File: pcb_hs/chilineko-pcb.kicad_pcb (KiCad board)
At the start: 2 copper layers, 303.8 x 94.2 mm, 178 parts, among them J1 JST SH 4-pin, J2 AVR-ISP-6, J3 DATA Breakout, J4 VBUS Breakout, SW1 Reset, U1 SRV05-4, U2 ATmega32U4-AU, Y1 16MHz

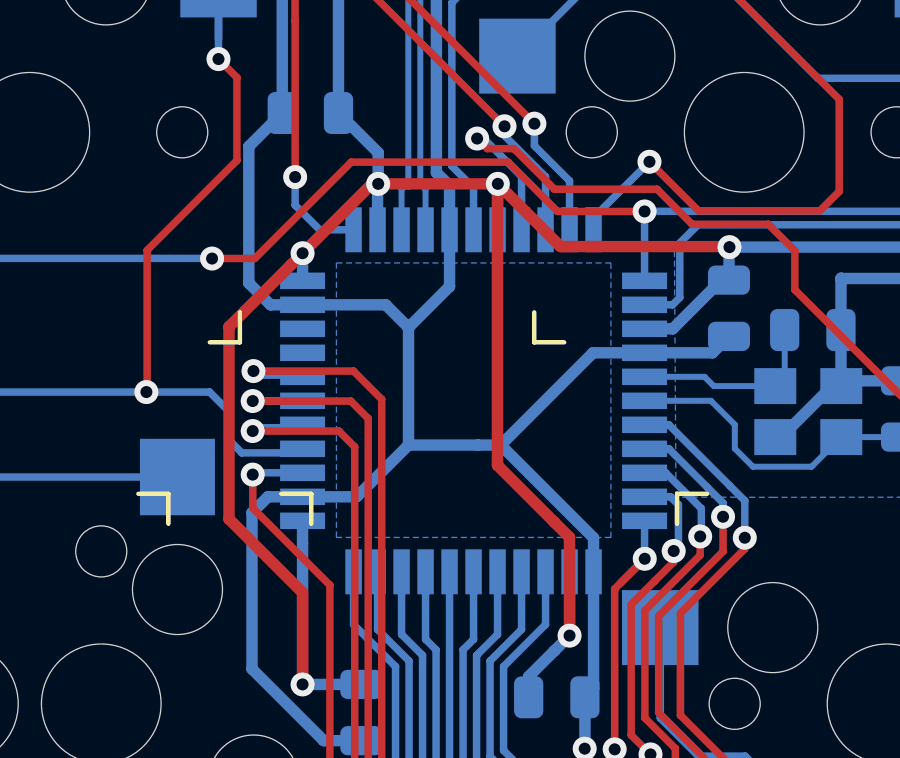
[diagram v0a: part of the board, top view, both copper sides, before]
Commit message: Update of PCB
Addition of double footprint for MCU. Now the board can be populated with both ATMEGA32U4-AU and ATMEGA32U4-MU.
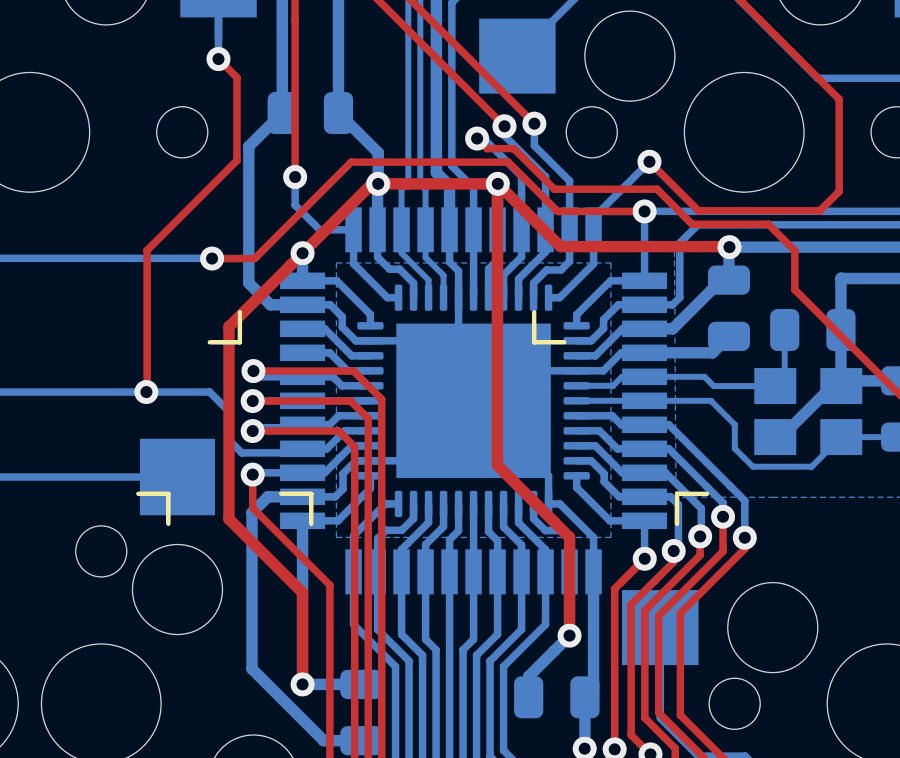
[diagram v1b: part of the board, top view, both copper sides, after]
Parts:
- added MU: QFN-44-1EP_7x7mm_P0.5mm_EP5.15x5.15mm, Package_DFN_QFN:QFN-44-1EP_7x7mm_P0.5mm_EP5.15x5.15mm, B.Cu at (28.6, 37.0)
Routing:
- net +5V: track 115.1 -> 132.3 mm
- net GND: track 189.8 -> 193.9 mm
- net Net-(R4-Pad2): track 14.6 -> 17.7 mm
- net COL11: track 338.8 -> 341.9 mm
- net MISO: track 61.2 -> 64.3 mm
- net ROW0: track 293.8 -> 296.9 mm
- net ROW1: track 302.9 -> 306.0 mm
- net COL3: track 141.9 -> 145.0 mm
- net MOSI: track 38.7 -> 41.8 mm
- net RESET: track 90.7 -> 93.6 mm
- net COL12: track 355.9 -> 358.8 mm
- net COL10: track 271.3 -> 274.0 mm
- net COL4: track 159.9 -> 162.6 mm
- net /MCU_D-: track 18.4 -> 21.1 mm
- net Net-(U2-Pad42): track 0.00 -> 2.64 mm
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
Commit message: Update to include HS socket in assembly files
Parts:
- MX1, MX10, MX11, MX12, MX13, MX14, MX15, MX16, MX17, MX18, MX19, MX2, MX20, MX21, MX22, MX23, MX24, MX25, MX26, MX27, MX28, MX29, MX3, MX30, MX31, MX32, MX33, MX34, MX35, MX36, MX37, MX38, MX39, MX4, MX40, MX41, MX42, MX43, MX44, MX45, MX46, MX47, MX48, MX49, MX5, MX50, MX51, MX52, MX53, MX54, MX55, MX56, MX57, MX58, MX59, MX6, MX60, MX61, MX62, MX63, MX64, MX65, MX66, MX67, MX68, MX69, MX7, MX70, MX71, MX72, MX73, MX74, MX75, MX76, MX77, MX78, MX79, MX8, MX9: footprint Keyswitches:Kailh_socket_MX_flippin -> marbastlib-mx:SW_MX_HS_1u; moved to B.Cu
- turned MX1 to 180 degrees
- turned MX10 to 180 degrees
- turned MX11 to 180 degrees
- turned MX12 to 180 degrees
- turned MX13 to 180 degrees
- turned MX14 to 0 degrees
- turned MX15 to 0 degrees
- turned MX16 to 180 degrees
- turned MX17 to 180 degrees
- turned MX18 to 180 degrees
- turned MX19 to 180 degrees
- turned MX2 to 180 degrees
- turned MX20 to 180 degrees
- turned MX21 to 180 degrees
- turned MX22 to 180 degrees
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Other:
- net class D removed
- net class Default removed
- net class Power removed
